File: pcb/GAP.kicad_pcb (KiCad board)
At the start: 2 copper layers, 76 x 47 mm, 103 parts, among them J1 USB_C_Receptacle, J2 Conn_01x02_Pin, J3 Conn_01x06_Socket, J4 Conn_01x05_Socket, Q1 BSP613, Q2 2N7002E, Q3 2N7002E, Q4 2N7002E, Q5 2N7002E, Q6 2N7002E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

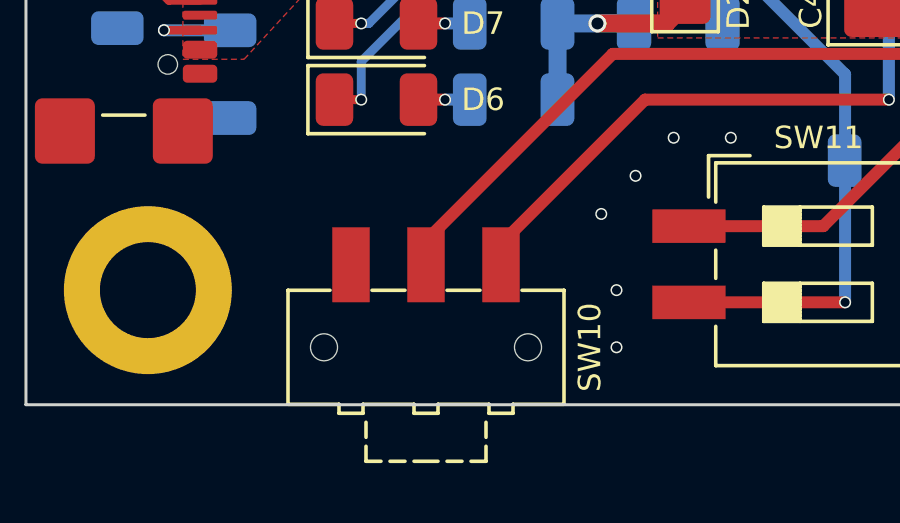
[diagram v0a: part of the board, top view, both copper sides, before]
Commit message: Change SW10 library
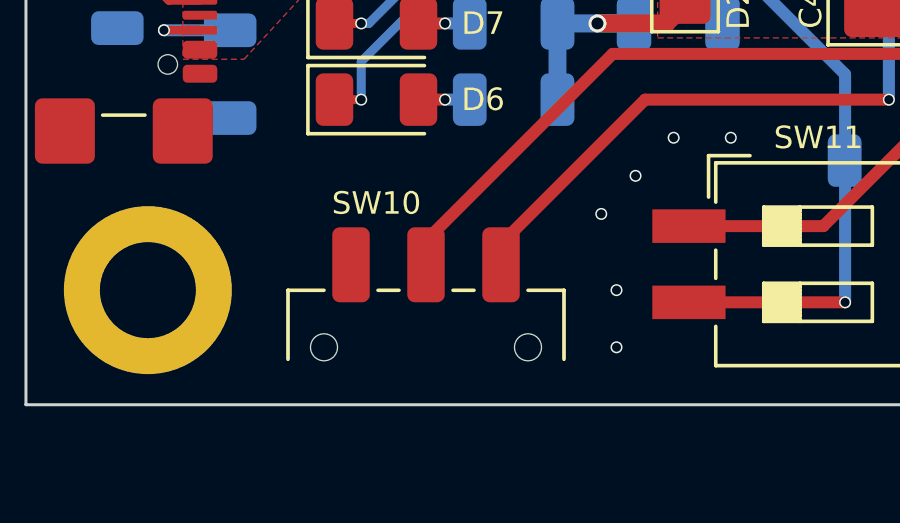
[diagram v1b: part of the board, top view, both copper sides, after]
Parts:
- SW10: footprint Button_Switch_SMD:SW_SPDT_CK-JS102011SAQN -> Button_Switch_SMD:SW_SPDT_CK_JS102011SAQN

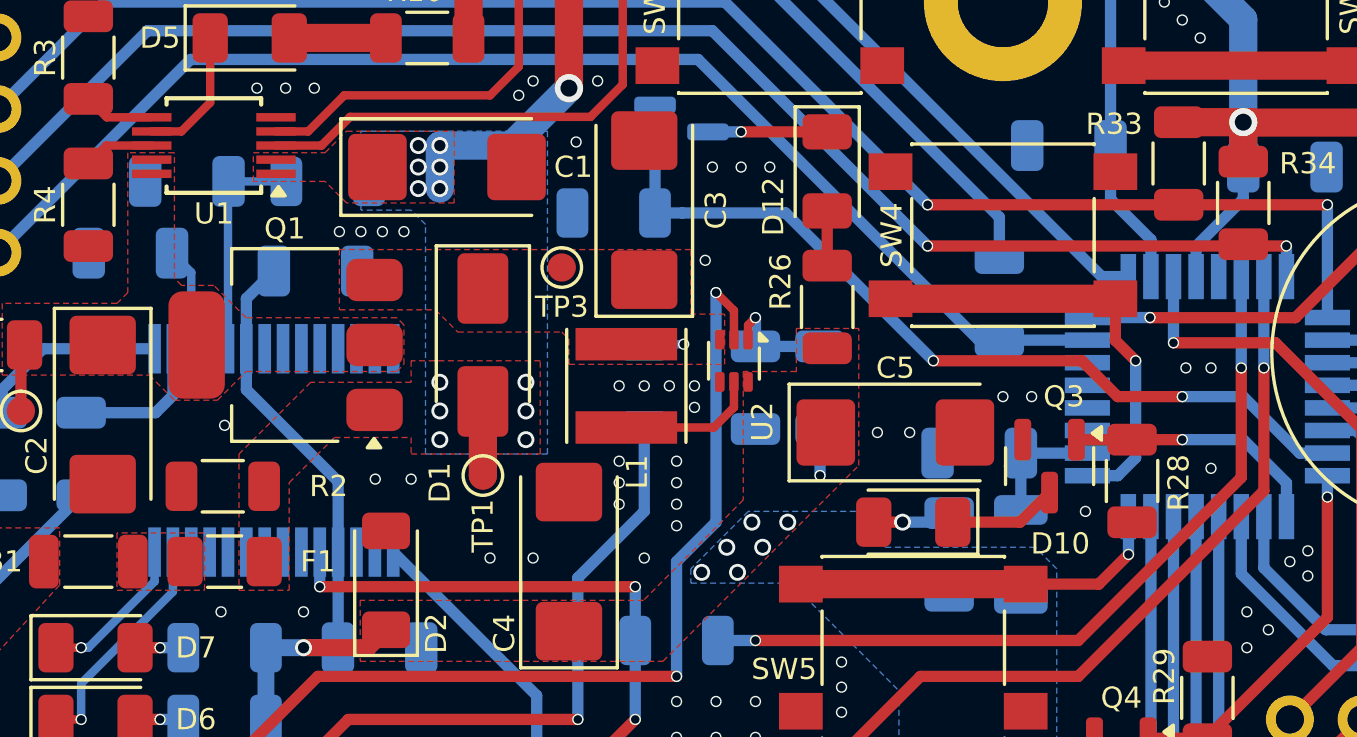
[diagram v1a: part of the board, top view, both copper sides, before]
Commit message: Add RTS/CTS to UART interface
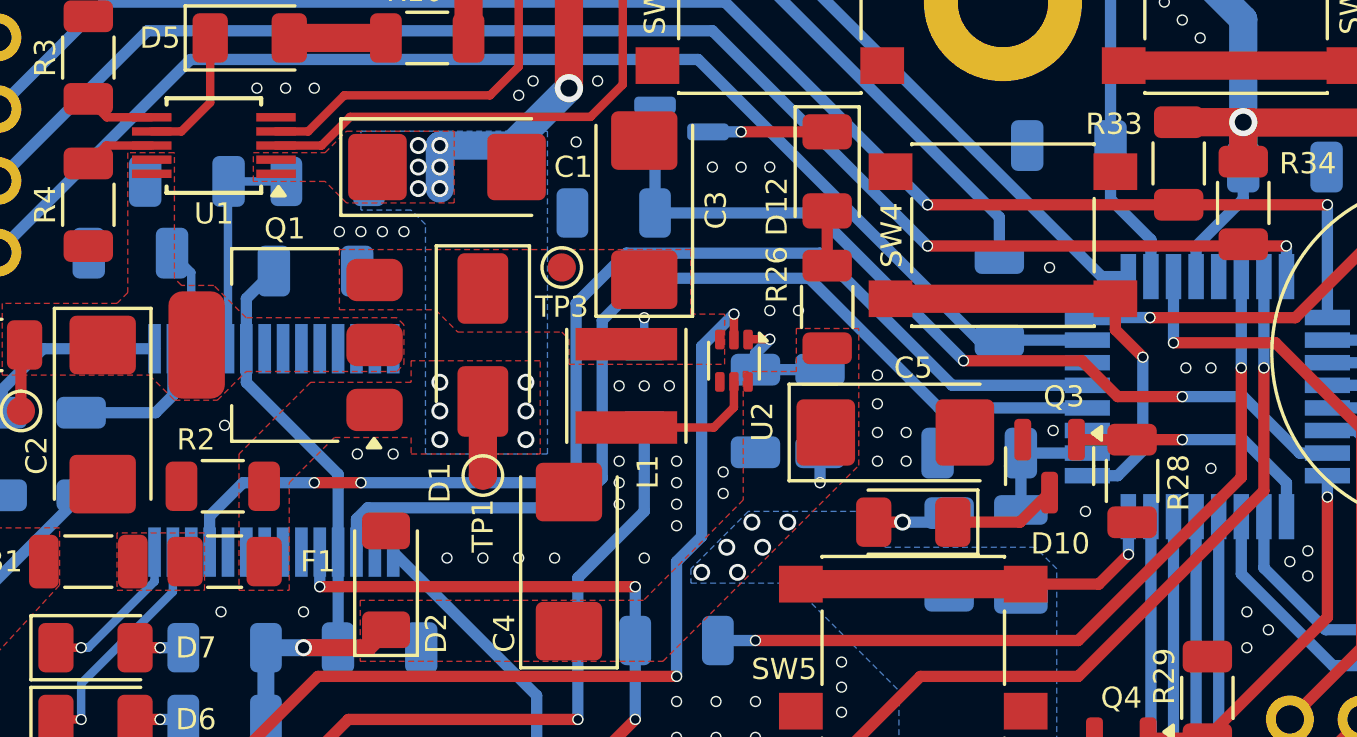
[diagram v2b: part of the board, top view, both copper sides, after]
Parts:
- moved R1 0.82 mm to (151.6, 95.8)
- moved R7 0.82 mm to (149.4, 95.8)
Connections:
- U3 pad 11: unconnected-(U3-CTS-Pad11) -> RTS
- U3 pad 3: unconnected-(U3-RTS-Pad3) -> CTS
- U4 pad 20: unconnected-(U4-PF0/TOSC1-Pad20) -> CTS
- U4 pad 21: unconnected-(U4-PF1/TOSC2-Pad21) -> RTS
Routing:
- net RTS: track 0.00 -> 41.6 mm, vias 0 -> 2
- net CTS: track 0.00 -> 35.8 mm
- net Net-(SW10-B): track 38.4 -> 36.9 mm
- net +5V: track 145.3 -> 144.8 mm
- net GND: vias 130 -> 137
